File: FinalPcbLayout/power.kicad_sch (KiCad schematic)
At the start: 38 parts, among them J3 Barrel_Jack, Q1 NMOS, Q4 PMOS, Q5 PMOS, U3 TPS63070RNMR, U4 AMS1117-3.3, U5 LM51551DSSR

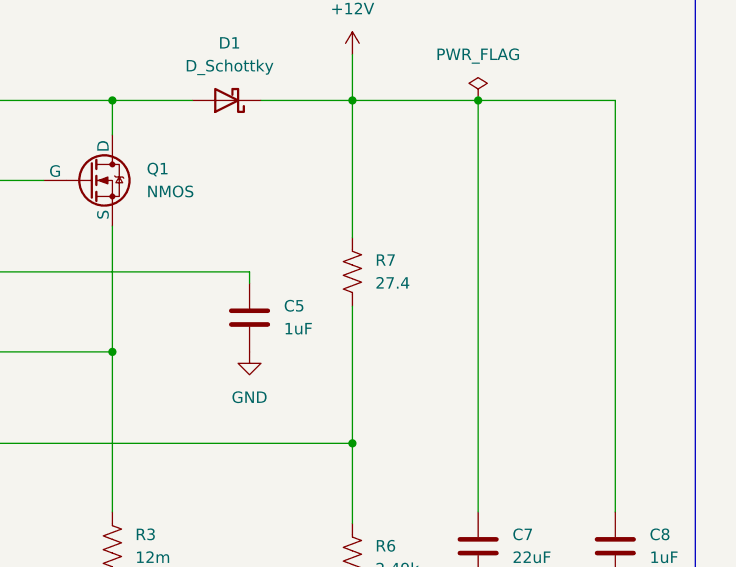
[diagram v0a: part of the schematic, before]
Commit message: Fixed Wrong Resistor
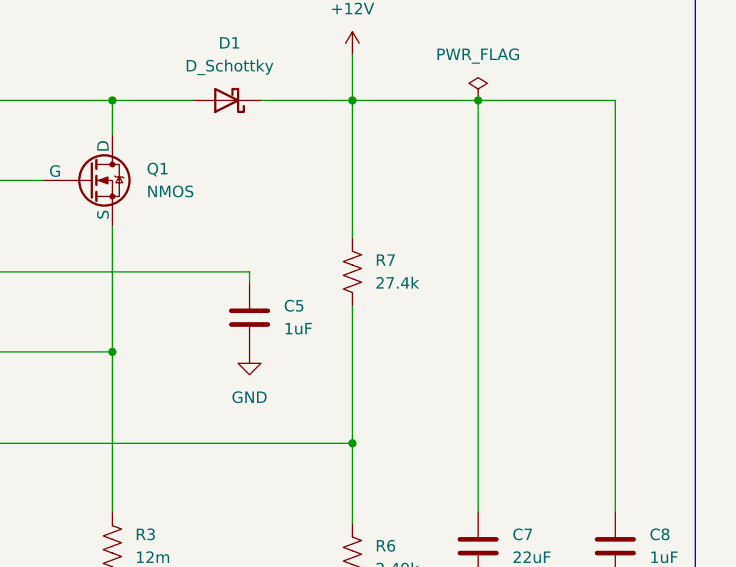
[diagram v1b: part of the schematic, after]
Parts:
- R7: value 27.4 -> 27.4k
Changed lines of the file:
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@@
       (effects (font (size 1.27 1.27)) (justify right))
     )
-    (property "Value" "27.4" (at 247.65 49.53 0)
+    (property "Value" "27.4k" (at 247.65 49.53 0)
       (effects (font (size 1.27 1.27)) (justify right))
     )

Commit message: Updated CSV
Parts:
- C1, C17, C2: digikey_pn (none) -> 1276-CL10E104KC8VPNCDKR-ND
- C10, C16, C18, C9: digikey_pn (none) -> 1276-1096-6-ND
- C11: digikey_pn (none) -> 1276-7076-1-ND
- C19: digikey_pn (none) -> 1276-1852-1-ND
- C3: digikey_pn (none) -> 399-C0603C682K5TACAUTODKR-ND
- C4: digikey_pn (none) -> 13-CC1812KKX7RBBB153DKR-ND
- C5, C8: digikey_pn (none) -> 1276-1102-6-ND
- C6: digikey_pn (none) -> 399-16643-6-ND
- C7: symbol Device:C -> Device:C_Polarized_US; digikey_pn (none) -> 493-9831-6-ND
- D7: digikey_pn (none) -> 160-1447-6-ND
- J3: digikey_pn (none) -> 2073-DCJ200-10-A-K1-K-ND
- L1: footprint Inductor_SMD:L_Coilcraft_XAL8050-223 -> Inductor_SMD:L_Coilcraft_XAL8080-XXX; Cost 0 -> 6.73; digikey_pn (none) -> 2457-XAL8080-222MED-ND
- L2: value L -> 2.2uH; footprint Inductor_SMD:L_Coilcraft_XAL8050-223 -> Inductor_SMD:L_Coilcraft_XAL8080-XXX; Cost 0 -> 6.73; digikey_pn (none) -> 2457-XAL8080-222MED-ND
- R1: digikey_pn (none) -> 13-RC0603JR-133K3LCT-ND
- R10: digikey_pn (none) -> RMCF0603FT523KCT-ND
- R11, R12: digikey_pn (none) -> RMCF0603FT100KCT-ND
- R13: value 10k -> 10k 1%; digikey_pn (none) -> RMCF0603FT10K0CT-ND
- R2: digikey_pn (none) -> RMCF0603FT21K0CT-ND
- R25: digikey_pn (none) -> 311-100CRCT-ND
- R3: digikey_pn (none) -> P0.012BVCT-ND
- R4: digikey_pn (none) -> 2019-RK73H2BTTD4870FCT-ND
- R5: footprint Resistor_SMD:R_0603_1608Metric -> Resistor_SMD:R_0805_2012Metric; digikey_pn (none) -> 311-100CRCT-ND
- R6: digikey_pn (none) -> P2.49KDBCT-ND
- R7: digikey_pn (none) -> RMCF0603FT27K4CT-ND
- U3: digikey_pn (none) -> 296-44874-1-ND
- U4: value AMS1117-3.3 -> LDI1117-3.3H; digikey_pn (none) -> 4878-LDI1117-3.3HCT-ND
- U5: digikey_pn (none) -> 296-LM51551DSSRCT-ND
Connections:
- net +12V: now also C7.1; no longer C7.2
- net GND: now also C7.2; no longer C7.1

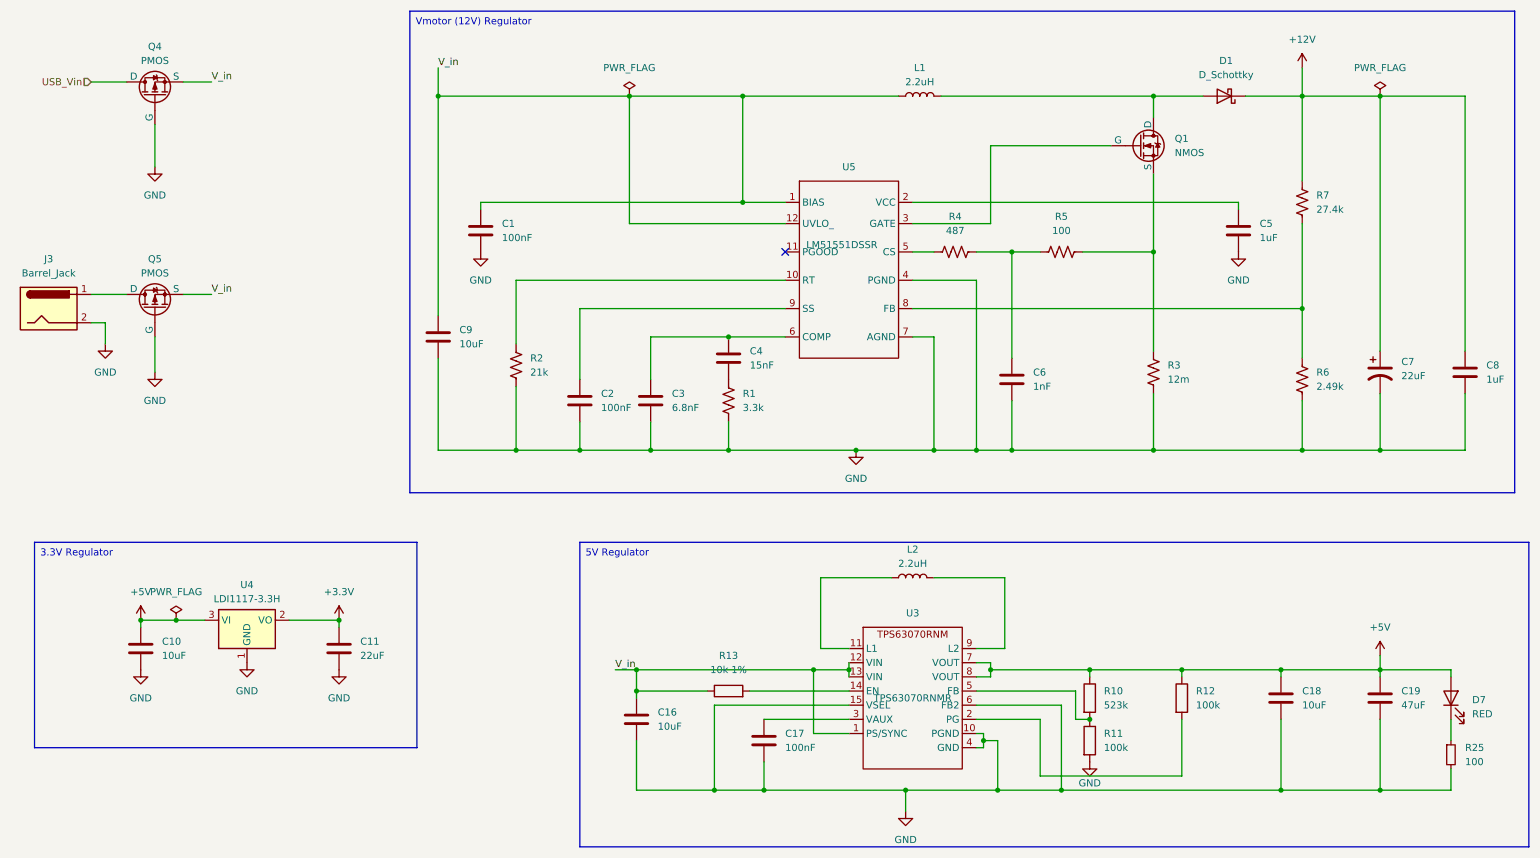
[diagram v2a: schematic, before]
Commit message: Axed Several Broken & Unused Parts
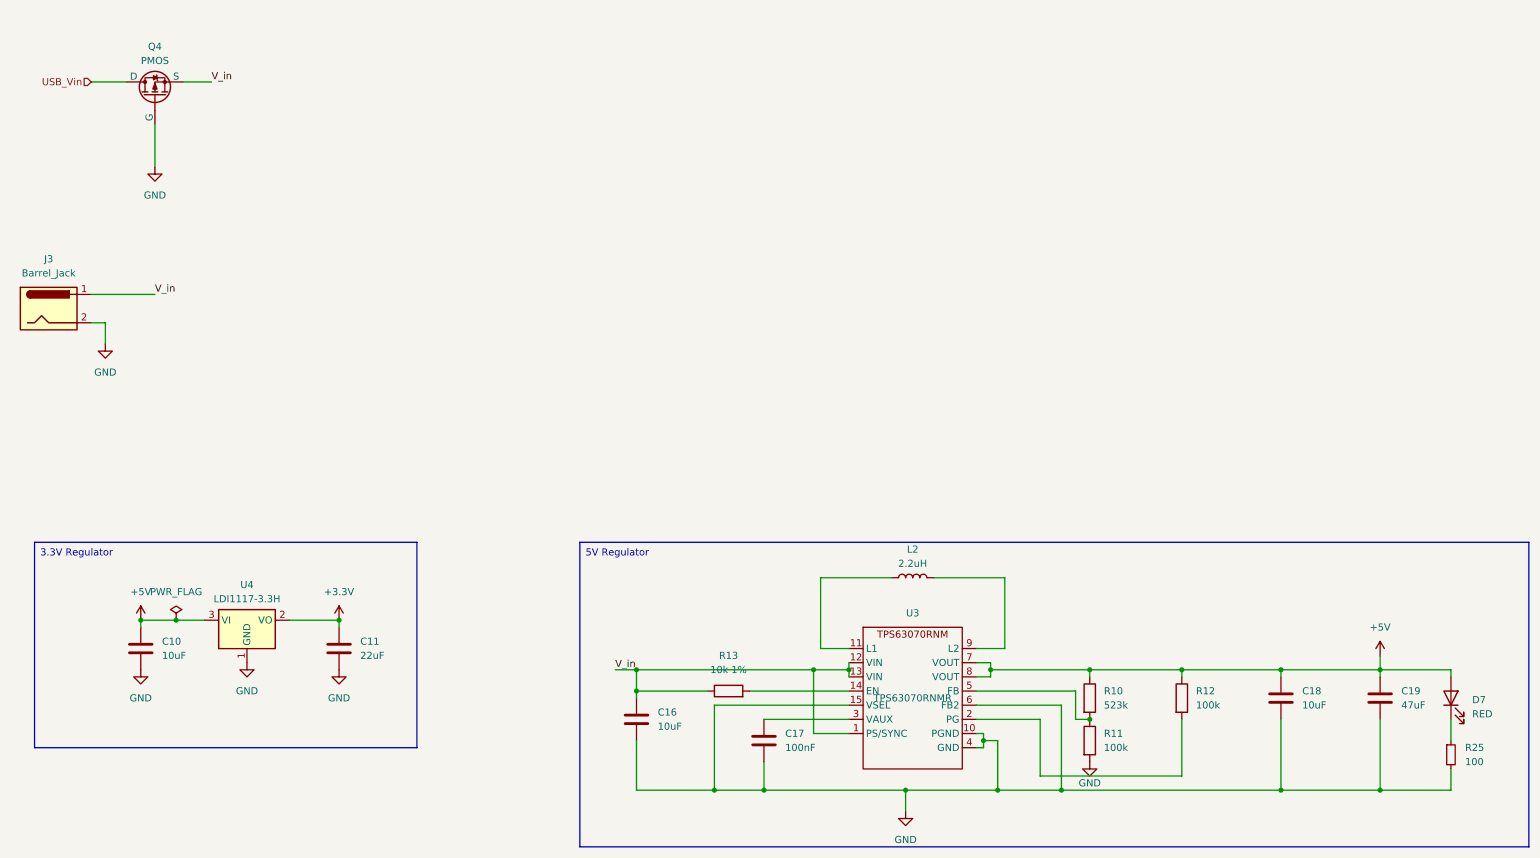
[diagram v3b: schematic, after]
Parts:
- removed C1, C2: 100nF, Capacitor_SMD:C_0603_1608Metric, symbol Device:C
- removed C3: 6.8nF, Capacitor_SMD:C_0603_1608Metric, symbol Device:C
- removed C4: 15nF, Capacitor_SMD:C_1812_4532Metric, symbol Device:C
- removed C5, C8: 1uF, Capacitor_SMD:C_0603_1608Metric, symbol Device:C
- removed C6: 1nF, Capacitor_SMD:C_0805_2012Metric, symbol Device:C
- removed C7: 22uF, Capacitor_SMD:C_Elec_4x5.4, symbol Device:C_Polarized_US
- removed C9: 10uF, Capacitor_SMD:C_0805_2012Metric, symbol Device:C
- removed D1: D_Schottky, SL42_E3_57T:CR_2-E3&slash_57T_VIS, symbol Device:D_Schottky
- removed L1: 2.2uH, Inductor_SMD:L_Coilcraft_XAL8080-XXX, symbol Device:L
- removed Q1: NMOS, Package_SON:WSON-8-1EP_2x2mm_P0.5mm_EP0.9x1.6mm, symbol Simulation_SPICE:NMOS
- removed Q5: PMOS, Package_TO_SOT_SMD:Vishay_PowerPAK_SC70-6L_Single, symbol OSMI-parts:SIA461DJ-T1-GE3
- removed R1: 3.3k, Resistor_SMD:R_0603_1608Metric, symbol Device:R_US
- removed R2: 21k, Resistor_SMD:R_0603_1608Metric, symbol Device:R_US
- removed R3: 12m, Resistor_SMD:R_1206_3216Metric, symbol Device:R_US
- removed R4: 487, Resistor_SMD:R_1206_3216Metric, symbol Device:R_US
- removed R5: 100, Resistor_SMD:R_0805_2012Metric, symbol Device:R_US
- removed R6: 2.49k, Resistor_SMD:R_0603_1608Metric, symbol Device:R_US
- removed R7: 27.4k, Resistor_SMD:R_0603_1608Metric, symbol Device:R_US
- removed U5: LM51551DSSR, Package_SON:WSON-12-1EP_3x2mm_P0.5mm_EP1x2.65_ThermalVias, symbol OSMI-parts:LM51551DSS
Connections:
- net V_in: now also J3.1
- no-connect marks 1 -> 0

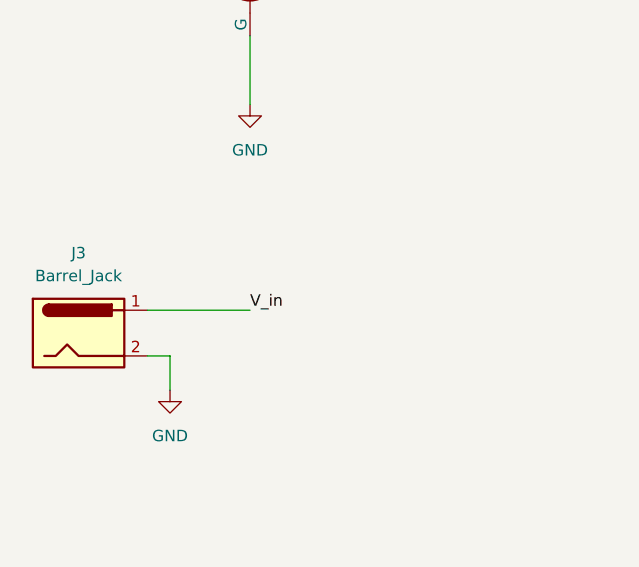
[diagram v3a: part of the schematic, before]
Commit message: Found A Good USB-To-Uart
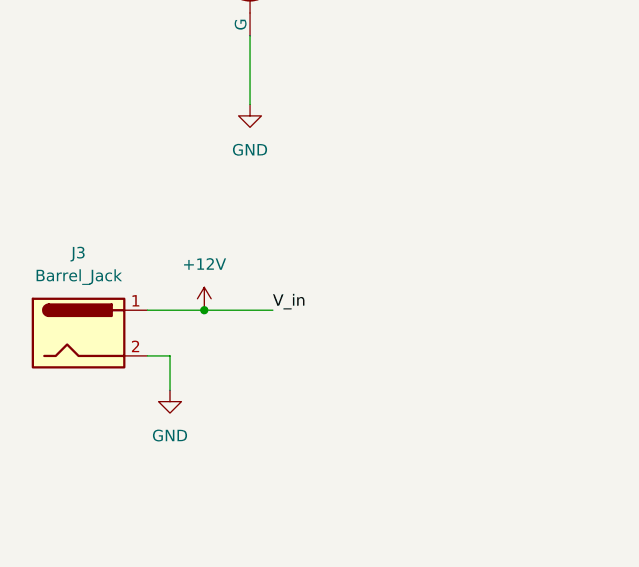
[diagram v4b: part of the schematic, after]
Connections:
- net V_in renamed +12V
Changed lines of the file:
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@@
   (junction (at 189.23 132.08) (diameter 0) (color 0 0 0 0)
   )
+  (junction (at 34.29 64.77) (diameter 0) (color 0 0 0 0)
+  )
   (junction (at 190.5 153.67) (diameter 0) (color 0 0 0 0)
   )
@@
     (stroke (width 0) (type default))
   )
-  (wire (pts (xy 27.94 64.77) (xy 39.37 64.77))
-    (stroke (width 0) (type default))
-  )
   (wire (pts (xy 190.5 153.67) (xy 201.93 153.67))
     (stroke (width 0) (type default))
@@
     (stroke (width 0) (type default))
   )
+  (wire (pts (xy 30.48 69.85) (xy 30.48 73.66))
+    (stroke (width 0) (type default))
+  )
   (wire (pts (xy 157.48 132.08) (xy 125.73 132.08))
     (stroke (width 0) (type default))
@@
     (stroke (width 0) (type default))
   )
+  (wire (pts (xy 27.94 64.77) (xy 34.29 64.77))
+    (stroke (width 0) (type default))
+  )
   (wire (pts (xy 201.93 138.43) (xy 201.93 153.67))
     (stroke (width 0) (type default))
@@
     (stroke (width 0) (type default))
   )
-  (wire (pts (xy 30.48 69.85) (xy 30.48 73.66))
-    (stroke (width 0) (type default))
-  )
   (wire (pts (xy 186.69 130.81) (xy 189.23 130.81))
     (stroke (width 0) (type default))
@@
   )
   (wire (pts (xy 27.94 69.85) (xy 30.48 69.85))
+    (stroke (width 0) (type default))
+  )
+  (wire (pts (xy 34.29 64.77) (xy 41.91 64.77))
     (stroke (width 0) (type default))
   )
@@
     (effects (font (size 1.27 1.27)) (justify left top))
   )
-  (label "V_in" (at 39.37 64.77 0) (fields_autoplaced)
+  (label "V_in" (at 41.91 64.77 0) (fields_autoplaced)
     (effects (font (size 1.27 1.27)) (justify left bottom))
   )
@@
         )
       )
+    )
+  )
+  (symbol (lib_id "power:+12V") (at 34.29 64.77 0) (unit 1)
+    (in_bom yes) (on_board yes) (dnp no) (fields_autoplaced)
+    (property "Reference" "#PWR02" (at 34.29 68.58 0)
+      (effects (font (size 1.27 1.27)) hide)
+    )
+    (property "Value" "+12V" (at 34.29 59.69 0)
+      (effects (font (size 1.27 1.27)))
+    )
+    (property "Footprint" "" (at 34.29 64.77 0)
+      (effects (font (size 1.27 1.27)) hide)
+    )
+    (property "Datasheet" "" (at 34.29 64.77 0)
+      (effects (font (size 1.27 1.27)) hide)
+    )
+    (pin "1")
+    (instances
+      (project "FinalPcbLayout"
+        (path "/9fcc273e-b318-4ade-b4c7-fe4ddbf9d677/c9a1ad6e-0e94-4050-a244-9bb2ec345a35"
+          (reference "#PWR02") (unit 1)
+        )
+      )

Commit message: Working on USB to UART
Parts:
- added D1: D_Schottky, Diode_SMD:D_SMA, symbol Device:D_Schottky
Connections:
- net +5V: now also D1.2 (A); no longer U4.3 (VI)
- new net D1-U4: D1.1 (K), U4.3 (VI)
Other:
- moved on the sheet: C10
